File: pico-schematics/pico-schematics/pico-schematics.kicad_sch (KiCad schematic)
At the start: 0 parts

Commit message: Completed V1.0 of the circuit diagram (implemented in person aswell), pico program adjusted also
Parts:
- added C1: 10u, symbol Device:C
- added D1: LED, symbol Device:LED
- added R1: 330R, symbol Device:R
- added R2, R3: 100R, symbol Device:R
- added SW1: SW_Push, symbol Switch:SW_Push
- added U1: Pico, RPi_Pico:RPi_Pico_SMD_TH, symbol MCU_RaspberryPi_and_Boards:Pico
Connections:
- new net: R2.1, R3.2, SW1.1
- new net: C1.1, R2.2
- new net: D1.1 (K), R1.1
- new net: D1.2 (A), U1.2 (GPIO1)
- new net: R3.1, U1.1 (GPIO0)
- new net +3V3: SW1.2, U1.39 (VSYS)
- new net GND: C1.2, R1.2, U1.28 (GND)

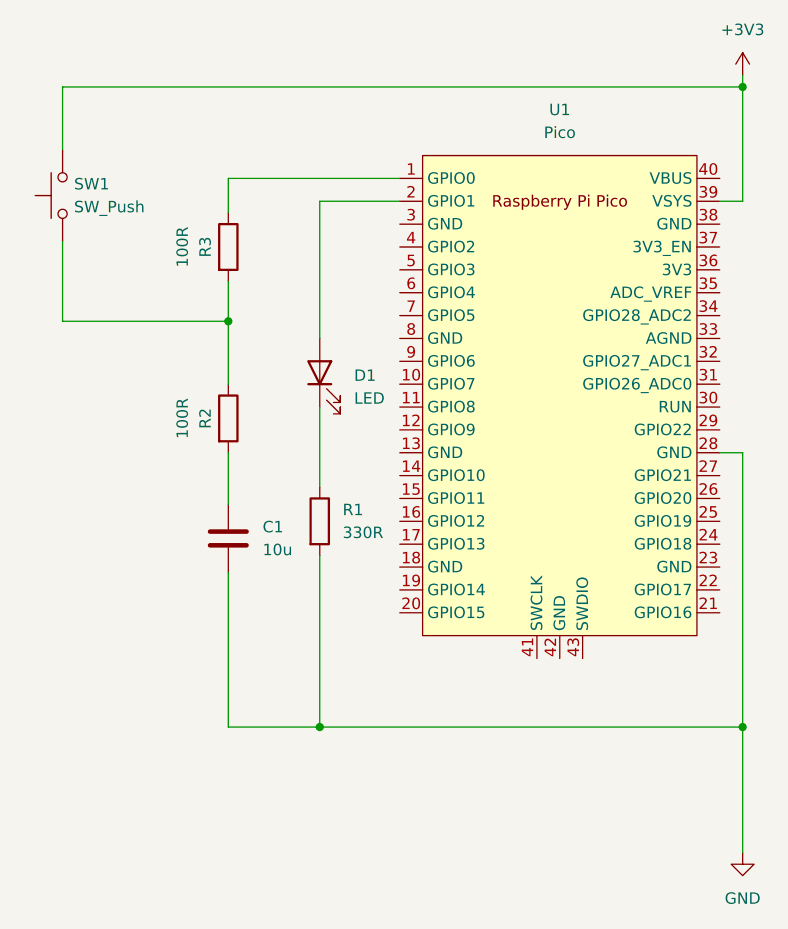
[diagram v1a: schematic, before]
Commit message: Compeleted V1.0 of Pi Pico software to handle button pushes and communicating that data over a serial connection (USB)
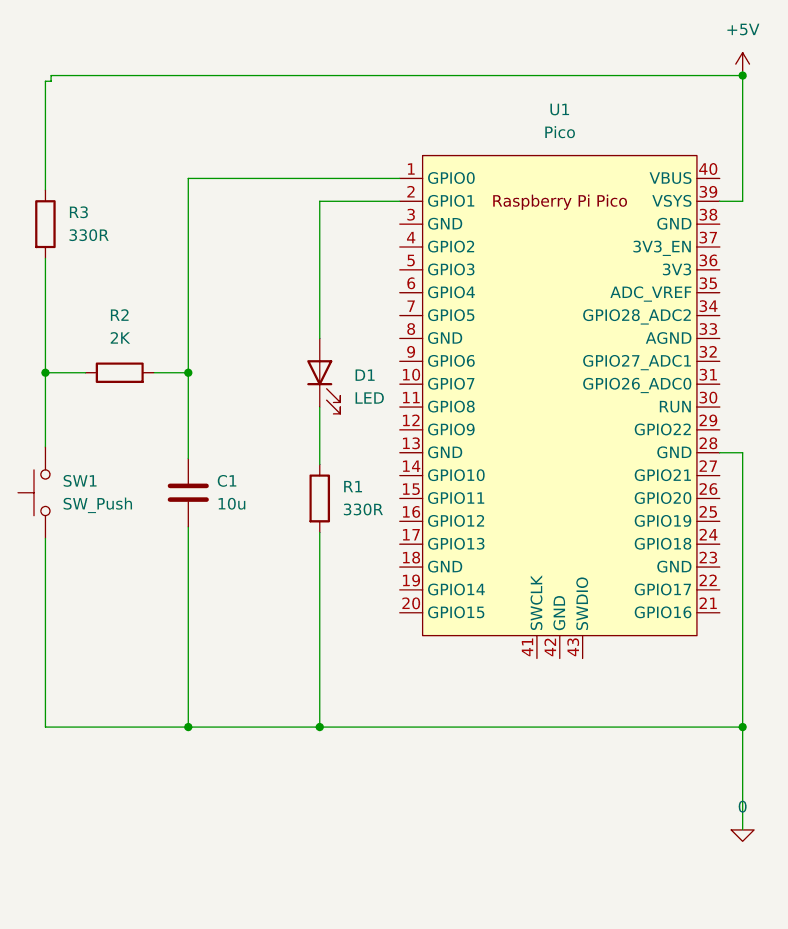
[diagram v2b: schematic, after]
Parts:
- R2: value 100R -> 2K
- R3: value 100R -> 330R
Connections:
- net at R2.1, R3.2: now also SW1.2; no longer SW1.1
- net at C1.1, R2.2: now also U1.1 (GPIO0)
- net +5V: now reaches R3.1
- net +5V: now also U1.39 (VSYS); no longer U1.1 (GPIO0)
- removed net +3V3: SW1.2, U1.39 (VSYS)
- net GND renamed 0
- net 0: now also SW1.1
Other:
- moved on the sheet: R1
